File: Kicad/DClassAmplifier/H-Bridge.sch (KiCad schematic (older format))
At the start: 9 parts

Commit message: Finish off Main Part of Schematic
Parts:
- removed C?: 1uF, Capacitor_SMD:C_0805_2012Metric_Pad1.18x1.45mm_HandSolder, symbol Device:C_Small
- removed D?: US1B-13-F, Diode_SMD:D_SMA_Handsoldering, symbol Device:D_Small
- removed R?: 10R, symbol Device:R_Small
- removed U?: 2ED21834S06JXUMA1, 2ED21834S:2ED21834S06JXUMA1, symbol 2ED21834S:2ED21834S06JXUMA1
- added C? (x3): 10u 50V, Capacitor_SMD:C_1206_3216Metric_Pad1.33x1.80mm_HandSolder, symbol Device:C_Small
- added IC? (x2): DGD05463FN-7, SON50P300X300X80-11N-D, symbol DGD05463FN-7:DGD05463FN-7
- added Q? (x2): PHP23NQ11T,127, Package_TO_SOT_THT:TO-220-3_Vertical, symbol Device:Q_NMOS_GDS
- added R?: 20k, Resistor_SMD:R_0603_1608Metric_Pad0.98x0.95mm_HandSolder, symbol Device:R_Small
- added R? (x3): 10, Resistor_SMD:R_2512_6332Metric_Pad1.40x3.35mm_HandSolder, symbol Device:R_Small
- C?: value 100nF 100V -> 10u 50V; footprint Capacitor_SMD:C_0805_2012Metric_Pad1.18x1.45mm_HandSolder -> Capacitor_SMD:C_1206_3216Metric_Pad1.33x1.80mm_HandSolder
- R?: value 10R -> 10; footprint (none) -> Resistor_SMD:R_2512_6332Metric_Pad1.40x3.35mm_HandSolder
- R?: value 10R -> 20k; footprint (none) -> Resistor_SMD:R_0603_1608Metric_Pad0.98x0.95mm_HandSolder; Notes Optional -> (none)
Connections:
- net labels added: INV_PWM, V_DT1, V_DT2, V_OUT+, V_OUT-
- net labels removed: HS_SOURCE, V_BOOTSTRAP, V_DT, V_OUT
- wire segments 37 -> 66
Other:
- note removed: "Bootstrap Circuit"
- moved on the sheet: C?, Q?, R?

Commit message: updates to schematic
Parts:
- added J3: Conn_01x03, symbol Connector_Generic:Conn_01x03
- added J4: Conn_01x02, symbol Connector_Generic:Conn_01x02
- IC1, IC2: renamed from IC?; footprint SON50P300X300X80-11N-D -> DGD05463:SON50P300X300X80-11N-D
- gave numbers to parts that had none: 14
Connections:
- net GND: now also J3.3 (Pin_3), J4.2 (Pin_2)
- net INV_PWM: now also J3.2 (Pin_2)
- net PWM: now also J3.1 (Pin_1)
- net VDD: now also J4.1 (Pin_1)

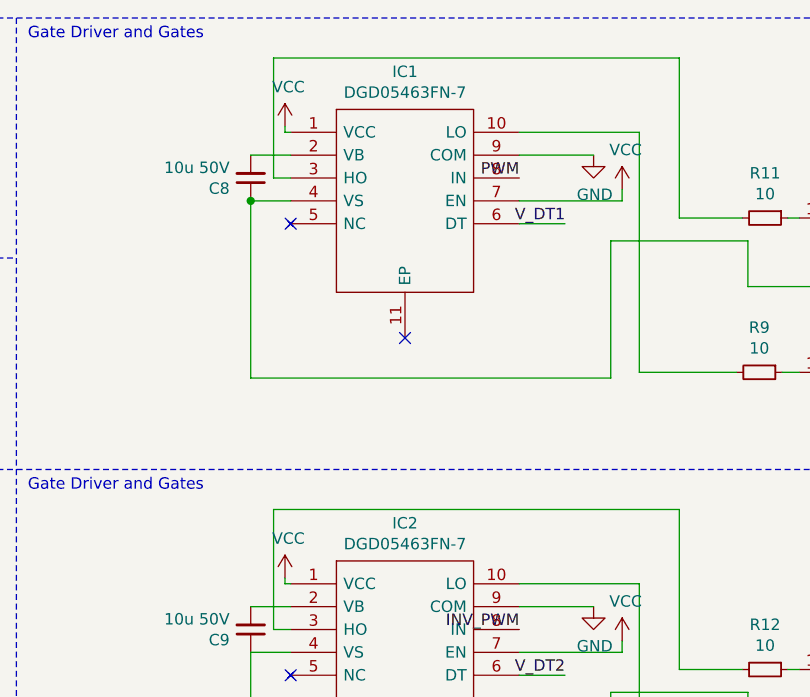
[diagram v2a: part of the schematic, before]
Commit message: Update Opamp for Input Filter
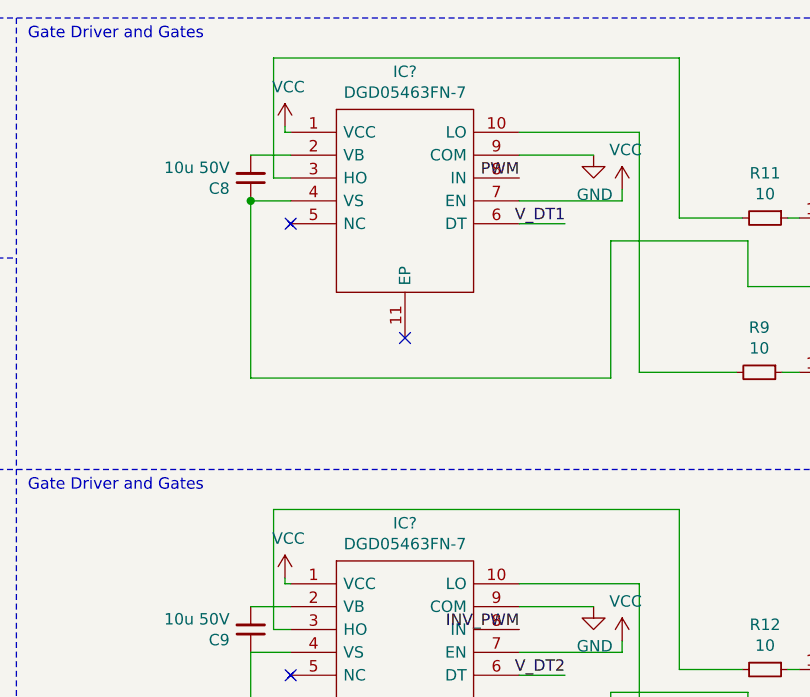
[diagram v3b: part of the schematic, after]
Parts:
- removed IC1, IC2: DGD05463FN-7, DGD05463:SON50P300X300X80-11N-D, symbol DGD05463FN-7:DGD05463FN-7
- added IC? (x2): DGD05463FN-7, SON50P300X300X80-11N-D, symbol DGD05463FN-7:DGD05463FN-7
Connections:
- net GND: now also IC?.9 (COM), IC?.9 (COM)
- net INV_PWM: now also IC?.8 (IN)
- net PWM: now also IC?.8 (IN)
- net VCC: now also IC?.1 (VCC), IC?.1 (VCC), IC?.7 (EN), IC?.7 (EN)
- net V_DT1: now also IC?.6 (DT)
- net V_DT2: now also IC?.6 (DT)
- net V_OUT+: now also IC?.4 (VS)
- net V_OUT-: now also IC?.4 (VS)
- net at R11.2: now also IC?.3 (HO)
- net at C8.2: now also IC?.2 (VB)
- net at R9.2: now also IC?.10 (LO)
- net at R10.2: now also IC?.10 (LO)
- net at C9.2: now also IC?.2 (VB)
- net at R12.2: now also IC?.3 (HO)
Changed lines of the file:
@@
 $Descr A4 11693 8268
 encoding utf-8
-Sheet 5 7
+Sheet 5 6
 Title ""
 Date ""
@@
 Wire Wire Line
 	4975 1775 4975 1750
-$Comp
-L DGD05463FN-7:DGD05463FN-7 IC1
-U 1 1 610F542B
-P 5000 1775
-F 0 "IC1" H 5500 2040 50  0000 C CNN
-F 1 "DGD05463FN-7" H 5500 1949 50  0000 C CNN
-F 2 "DGD05463:SON50P300X300X80-11N-D" H 5850 1875 50  0001 L CNN
-F 3 "https://www.diodes.com/assets/Datasheets/DGD05463.pdf" H 5850 1775 50  0001 L CNN
-F 4 "DiodesZetex DGD05463FN-7 Dual Half Bridge MOSFET Power Driver, 1.5 (Source) A, 2.5 (Sink) A 10-Pin, W-DFN3030" H 5850 1675 50  0001 L CNN "Description"
-F 5 "0.8" H 5850 1575 50  0001 L CNN "Height"
-F 6 "Diodes Inc." H 5850 1475 50  0001 L CNN "Manufacturer_Name"
-F 7 "DGD05463FN-7" H 5850 1375 50  0001 L CNN "Manufacturer_Part_Number"
-F 8 "621-DGD05463FN-7" H 5850 1275 50  0001 L CNN "Mouser Part Number"
-F 9 "https://www.mouser.com/Search/Refine.aspx?Keyword=621-DGD05463FN-7" H 5850 1175 50  0001 L CNN "Mouser Price/Stock"
-F 10 "DGD05463FN-7" H 5850 1075 50  0001 L CNN "Arrow Part Number"
-F 11 "https://www.arrow.com/en/products/dgd05463fn-7/diodes-incorporated" H 5850 975 50  0001 L CNN "Arrow Price/Stock"
-	1    5000 1775
-	1    0    0    -1
-$EndComp
 Wire Wire Line
 	7525 3025 7525 3075
@@
 Wire Wire Line
 	4975 3750 4975 3725
-$Comp
-L DGD05463FN-7:DGD05463FN-7 IC2
-U 1 1 6117AF51
-P 5000 3750
-F 0 "IC2" H 5500 4015 50  0000 C CNN
-F 1 "DGD05463FN-7" H 5500 3924 50  0000 C CNN
-F 2 "DGD05463:SON50P300X300X80-11N-D" H 5850 3850 50  0001 L CNN
-F 3 "https://www.diodes.com/assets/Datasheets/DGD05463.pdf" H 5850 3750 50  0001 L CNN
-F 4 "DiodesZetex DGD05463FN-7 Dual Half Bridge MOSFET Power Driver, 1.5 (Source) A, 2.5 (Sink) A 10-Pin, W-DFN3030" H 5850 3650 50  0001 L CNN "Description"
-F 5 "0.8" H 5850 3550 50  0001 L CNN "Height"
-F 6 "Diodes Inc." H 5850 3450 50  0001 L CNN "Manufacturer_Name"
-F 7 "DGD05463FN-7" H 5850 3350 50  0001 L CNN "Manufacturer_Part_Number"
-F 8 "621-DGD05463FN-7" H 5850 3250 50  0001 L CNN "Mouser Part Number"
-F 9 "https://www.mouser.com/Search/Refine.aspx?Keyword=621-DGD05463FN-7" H 5850 3150 50  0001 L CNN "Mouser Price/Stock"
-F 10 "DGD05463FN-7" H 5850 3050 50  0001 L CNN "Arrow Part Number"
-F 11 "https://www.arrow.com/en/products/dgd05463fn-7/diodes-incorporated" H 5850 2950 50  0001 L CNN "Arrow Price/Stock"
-	1    5000 3750
-	1    0    0    -1
-$EndComp
 Wire Wire Line
 	7525 5000 7525 5050
@@
 Text Label 6000 3950 2    50   ~ 0
 INV_PWM
+$Comp
+L DGD05463FN-7:DGD05463FN-7 IC?
+U 1 1 610FE89C
+P 5000 1775
+F 0 "IC?" H 5500 2040 50  0000 C CNN
+F 1 "DGD05463FN-7" H 5500 1949 50  0000 C CNN
+F 2 "SON50P300X300X80-11N-D" H 5850 1875 50  0001 L CNN
+F 3 "https://www.diodes.com/assets/Datasheets/DGD05463.pdf" H 5850 1775 50  0001 L CNN
+F 4 "DiodesZetex DGD05463FN-7 Dual Half Bridge MOSFET Power Driver, 1.5 (Source) A, 2.5 (Sink) A 10-Pin, W-DFN3030" H 5850 1675 50  0001 L CNN "Description"
+F 5 "0.8" H 5850 1575 50  0001 L CNN "Height"
+F 6 "Diodes Inc." H 5850 1475 50  0001 L CNN "Manufacturer_Name"
+F 7 "DGD05463FN-7" H 5850 1375 50  0001 L CNN "Manufacturer_Part_Number"
+F 8 "621-DGD05463FN-7" H 5850 1275 50  0001 L CNN "Mouser Part Number"
+F 9 "https://www.mouser.com/Search/Refine.aspx?Keyword=621-DGD05463FN-7" H 5850 1175 50  0001 L CNN "Mouser Price/Stock"
+F 10 "DGD05463FN-7" H 5850 1075 50  0001 L CNN "Arrow Part Number"
+F 11 "https://www.arrow.com/en/products/dgd05463fn-7/diodes-incorporated" H 5850 975 50  0001 L CNN "Arrow Price/Stock"
+	1    5000 1775
+	1    0    0    -1
+$EndComp
+$Comp
+L DGD05463FN-7:DGD05463FN-7 IC?
+U 1 1 612235BB
+P 5000 3750
+F 0 "IC?" H 5500 4015 50  0000 C CNN
+F 1 "DGD05463FN-7" H 5500 3924 50  0000 C CNN
+F 2 "SON50P300X300X80-11N-D" H 5850 3850 50  0001 L CNN
+F 3 "https://www.diodes.com/assets/Datasheets/DGD05463.pdf" H 5850 3750 50  0001 L CNN
+F 4 "DiodesZetex DGD05463FN-7 Dual Half Bridge MOSFET Power Driver, 1.5 (Source) A, 2.5 (Sink) A 10-Pin, W-DFN3030" H 5850 3650 50  0001 L CNN "Description"
+F 5 "0.8" H 5850 3550 50  0001 L CNN "Height"
+F 6 "Diodes Inc." H 5850 3450 50  0001 L CNN "Manufacturer_Name"
+F 7 "DGD05463FN-7" H 5850 3350 50  0001 L CNN "Manufacturer_Part_Number"
+F 8 "621-DGD05463FN-7" H 5850 3250 50  0001 L CNN "Mouser Part Number"
+F 9 "https://www.mouser.com/Search/Refine.aspx?Keyword=621-DGD05463FN-7" H 5850 3150 50  0001 L CNN "Mouser Price/Stock"
+F 10 "DGD05463FN-7" H 5850 3050 50  0001 L CNN "Arrow Part Number"
+F 11 "https://www.arrow.com/en/products/dgd05463fn-7/diodes-incorporated" H 5850 2950 50  0001 L CNN "Arrow Price/Stock"
+	1    5000 3750
+	1    0    0    -1
+$EndComp
 $EndSCHEMATC

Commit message: Added footprints to schematic
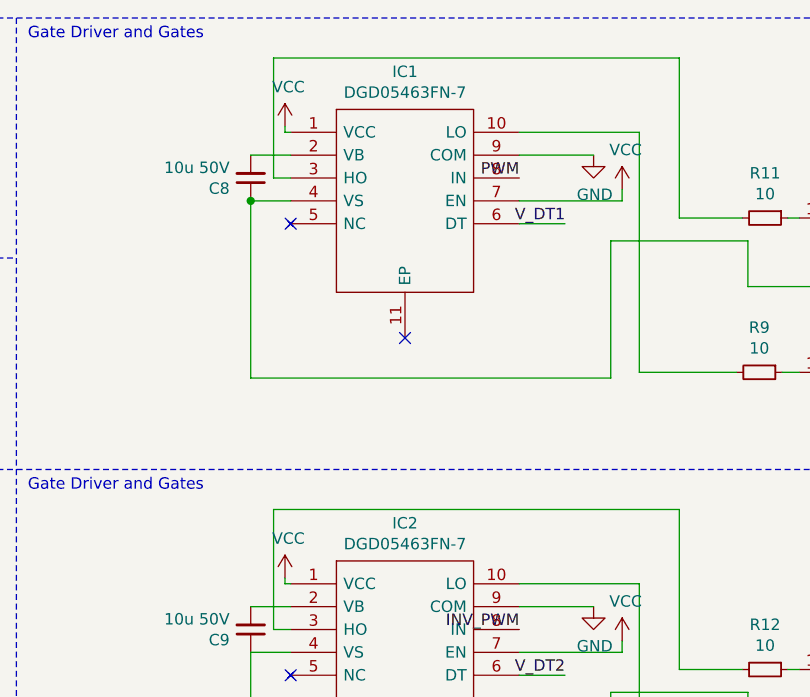
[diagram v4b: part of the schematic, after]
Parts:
- IC1, IC2: renamed from IC?; footprint SON50P300X300X80-11N-D -> DGD05463:SON50P300X300X80-11N-D
- J3: footprint (none) -> Connector_PinSocket_2.54mm:PinSocket_1x03_P2.54mm_Vertical
- J4: footprint (none) -> Connector_PinSocket_2.54mm:PinSocket_1x02_P2.54mm_Vertical
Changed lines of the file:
@@
 F 0 "J4" H 2030 3192 50  0000 L CNN
 F 1 "Conn_01x02" H 2030 3101 50  0000 L CNN
-F 2 "" H 1950 3200 50  0001 C CNN
+F 2 "Connector_PinSocket_2.54mm:PinSocket_1x02_P2.54mm_Vertical" H 1950 3200 50  0001 C CNN
 F 3 "~" H 1950 3200 50  0001 C CNN
 	1    1950 3200
@@
 F 0 "J3" H 2030 2592 50  0000 L CNN
 F 1 "Conn_01x03" H 2030 2501 50  0000 L CNN
-F 2 "" H 1950 2550 50  0001 C CNN
+F 2 "Connector_PinSocket_2.54mm:PinSocket_1x03_P2.54mm_Vertical" H 1950 2550 50  0001 C CNN
 F 3 "~" H 1950 2550 50  0001 C CNN
 	1    1950 2550
@@
 INV_PWM
 $Comp
-L DGD05463FN-7:DGD05463FN-7 IC?
+L DGD05463FN-7:DGD05463FN-7 IC1
 U 1 1 610FE89C
 P 5000 1775
-F 0 "IC?" H 5500 2040 50  0000 C CNN
+F 0 "IC1" H 5500 2040 50  0000 C CNN
 F 1 "DGD05463FN-7" H 5500 1949 50  0000 C CNN
-F 2 "SON50P300X300X80-11N-D" H 5850 1875 50  0001 L CNN
+F 2 "DGD05463:SON50P300X300X80-11N-D" H 5850 1875 50  0001 L CNN
 F 3 "https://www.diodes.com/assets/Datasheets/DGD05463.pdf" H 5850 1775 50  0001 L CNN
 F 4 "DiodesZetex DGD05463FN-7 Dual Half Bridge MOSFET Power Driver, 1.5 (Source) A, 2.5 (Sink) A 10-Pin, W-DFN3030" H 5850 1675 50  0001 L CNN "Description"
@@
 $EndComp
 $Comp
-L DGD05463FN-7:DGD05463FN-7 IC?
+L DGD05463FN-7:DGD05463FN-7 IC2
 U 1 1 612235BB
 P 5000 3750
-F 0 "IC?" H 5500 4015 50  0000 C CNN
+F 0 "IC2" H 5500 4015 50  0000 C CNN
 F 1 "DGD05463FN-7" H 5500 3924 50  0000 C CNN
-F 2 "SON50P300X300X80-11N-D" H 5850 3850 50  0001 L CNN
+F 2 "DGD05463:SON50P300X300X80-11N-D" H 5850 3850 50  0001 L CNN
 F 3 "https://www.diodes.com/assets/Datasheets/DGD05463.pdf" H 5850 3750 50  0001 L CNN
 F 4 "DiodesZetex DGD05463FN-7 Dual Half Bridge MOSFET Power Driver, 1.5 (Source) A, 2.5 (Sink) A 10-Pin, W-DFN3030" H 5850 3650 50  0001 L CNN "Description"

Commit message: Update Terminal Block Footprints
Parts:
- J3: footprint Connector_PinSocket_2.54mm:PinSocket_1x03_P2.54mm_Vertical -> TerminalBlock:TerminalBlock_bornier-3_P5.08mm
- J4: footprint Connector_PinSocket_2.54mm:PinSocket_1x02_P2.54mm_Vertical -> TerminalBlock:TerminalBlock_bornier-2_P5.08mm
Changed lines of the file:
@@
 F 0 "J4" H 2030 3192 50  0000 L CNN
 F 1 "Conn_01x02" H 2030 3101 50  0000 L CNN
-F 2 "Connector_PinSocket_2.54mm:PinSocket_1x02_P2.54mm_Vertical" H 1950 3200 50  0001 C CNN
+F 2 "TerminalBlock:TerminalBlock_bornier-2_P5.08mm" H 1950 3200 50  0001 C CNN
 F 3 "~" H 1950 3200 50  0001 C CNN
 	1    1950 3200
@@
 F 0 "J3" H 2030 2592 50  0000 L CNN
 F 1 "Conn_01x03" H 2030 2501 50  0000 L CNN
-F 2 "Connector_PinSocket_2.54mm:PinSocket_1x03_P2.54mm_Vertical" H 1950 2550 50  0001 C CNN
+F 2 "TerminalBlock:TerminalBlock_bornier-3_P5.08mm" H 1950 2550 50  0001 C CNN
 F 3 "~" H 1950 2550 50  0001 C CNN
 	1    1950 2550

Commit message: Added input to global schematic
Changed the sig_in net label in the LPF sheet to a hierarchical net label of the same name
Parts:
- IC1, IC2: symbol DGD05463FN-7:DGD05463FN-7 -> DClassAmplifier-rescue:DGD05463FN-7-DGD05463FN-7
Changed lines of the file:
@@
 INV_PWM
 $Comp
-L DGD05463FN-7:DGD05463FN-7 IC1
+L DClassAmplifier-rescue:DGD05463FN-7-DGD05463FN-7 IC1
 U 1 1 610FE89C
 P 5000 1775
@@
 $EndComp
 $Comp
-L DGD05463FN-7:DGD05463FN-7 IC2
+L DClassAmplifier-rescue:DGD05463FN-7-DGD05463FN-7 IC2
 U 1 1 612235BB
 P 5000 3750

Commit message: Combined Board
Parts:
- removed J3: Conn_01x03, TerminalBlock:TerminalBlock_bornier-3_P5.08mm, symbol Connector_Generic:Conn_01x03
- removed J4: Conn_01x02, TerminalBlock:TerminalBlock_bornier-2_P5.08mm, symbol Connector_Generic:Conn_01x02
- Q1, Q2, Q3, Q4: footprint Package_TO_SOT_THT:TO-220-3_Vertical -> Package_TO_SOT_THT:TO-220-3_Horizontal_TabDown
- renumbered C8 to C10, C7 to C11, C9 to C12, C6 to C9, R11 to R16, R7 to R17, R9 to R18, R12 to R19, R8 to R20, R10 to R21, IC1 to U2, IC2 to U3
